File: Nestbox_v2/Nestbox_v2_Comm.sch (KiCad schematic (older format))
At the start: 3 parts

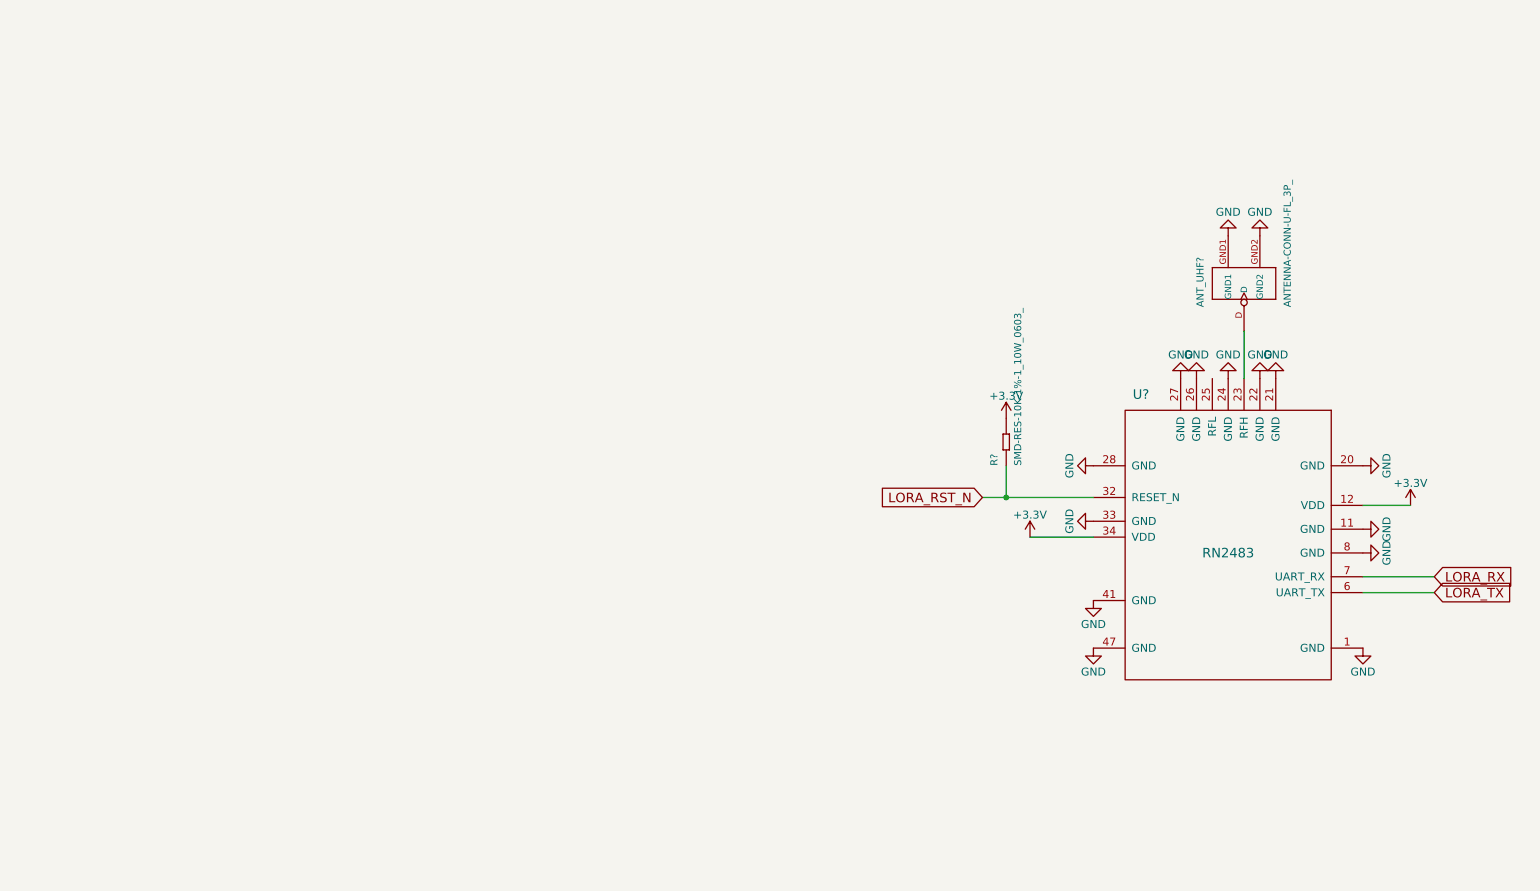
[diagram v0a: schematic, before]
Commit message: Adds XBee module to Communication schematic
The XBee module would be used for local data transfer, from a Nestbox to a
computer. This would allow data readout without the need to physically access
the box.
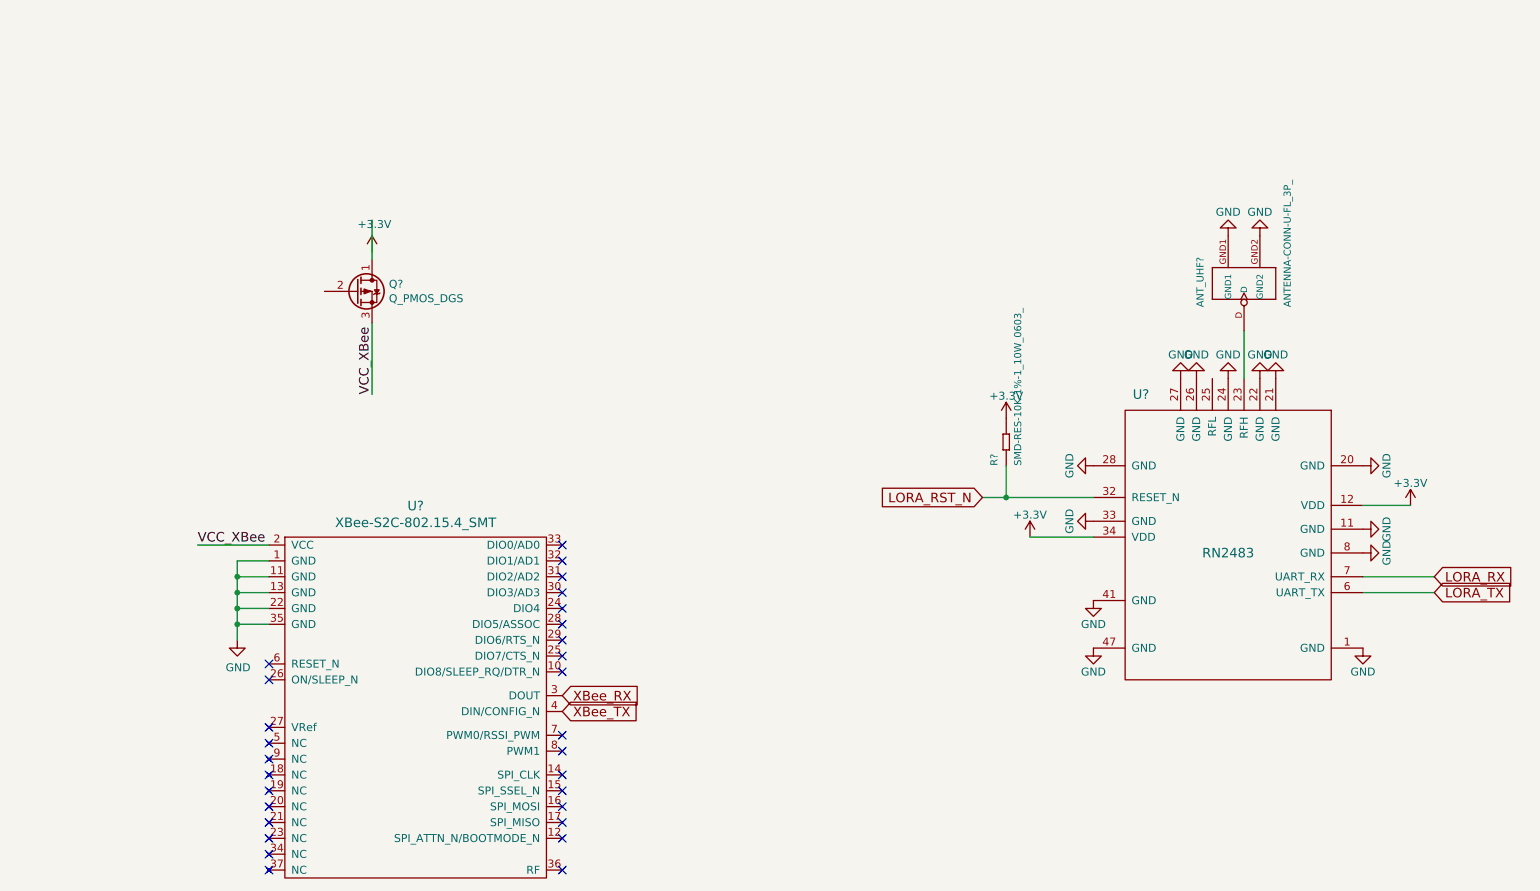
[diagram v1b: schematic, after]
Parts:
- added Q?: Q_PMOS_DGS, symbol Q_PMOS_DGS
- added U?: XBee-S2C-802.15.4_SMT, symbol XBee-S2C-802.15.4_SMT
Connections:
- net labels added: VCC_XBee, XBee_RX, XBee_TX
- wire segments 7 -> 21
- no-connect marks 0 -> 29
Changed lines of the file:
@@
 	7450 4150 7050 4150
 Wire Wire Line
-	6750 3900 7450 3900
+	6750 3900 6900 3900
+Wire Wire Line
+	6900 3900 7450 3900
 Text GLabel 6750 3900 0    60   Input ~ 0
 LORA_RST_N
@@
 	1    0    0    -1
 $EndComp
+NoConn ~ 4100 4200
+NoConn ~ 4100 4300
+NoConn ~ 4100 4400
+NoConn ~ 4100 4500
+NoConn ~ 4100 4600
+NoConn ~ 4100 4700
+NoConn ~ 4100 4800
+NoConn ~ 4100 4900
+NoConn ~ 4100 5000
+NoConn ~ 4100 5400
+NoConn ~ 4100 5500
+NoConn ~ 4100 5650
+NoConn ~ 4100 5750
+NoConn ~ 4100 5850
+NoConn ~ 4100 5950
+NoConn ~ 4100 6050
+NoConn ~ 4100 6250
+NoConn ~ 2250 5450
+NoConn ~ 2250 5550
+NoConn ~ 2250 5650
+NoConn ~ 2250 5750
+NoConn ~ 2250 5850
+NoConn ~ 2250 5950
+NoConn ~ 2250 6050
+NoConn ~ 2250 6150
+NoConn ~ 2250 6250
+NoConn ~ 2250 5350
+NoConn ~ 2250 5050
+NoConn ~ 2250 4950
+Wire Wire Line
+	2250 4300 2050 4300
+Wire Wire Line
+	2050 4300 2050 4400
+Wire Wire Line
+	2050 4400 2050 4500
+Wire Wire Line
+	2050 4500 2050 4600
+Wire Wire Line
+	2050 4600 2050 4700
+Wire Wire Line
+	2050 4700 2050 4800
+Wire Wire Line
+	2050 4400 2250 4400
+Wire Wire Line
+	2050 4500 2250 4500
+Connection ~ 2050 4400
+Wire Wire Line
+	2050 4600 2250 4600
+Connection ~ 2050 4500
+Wire Wire Line
+	2050 4700 2250 4700
+Connection ~ 2050 4600
+$Comp
+L GND #PWR?
+U 1 1 59FDFCD3
+P 2050 4800
+F 0 "#PWR?" H 2050 4550 50  0001 C CNN
+F 1 "GND" H 2055 4627 50  0000 C CNN
+F 2 "" H 2050 4800 50  0000 C CNN
+F 3 "" H 2050 4800 50  0000 C CNN
+	1    2050 4800
+	1    0    0    -1
+$EndComp
+Connection ~ 2050 4700
+Wire Wire Line
+	2250 4200 1800 4200
+Text Label 1800 4200 0    60   ~ 0
+VCC_XBee
+Text GLabel 4100 5150 2    60   Input ~ 0
+XBee_RX
+Text GLabel 4100 5250 2    60   Input ~ 0
+XBee_TX
+$Comp
+L XBee-S2C-802.15.4_SMT U?
+U 1 1 59FE0508
+P 2800 4100
+F 0 "U?" H 3175 4247 60  0000 C CNN
+F 1 "XBee-S2C-802.15.4_SMT" H 3175 4141 60  0000 C CNN
+F 2 "" H 2800 4100 60  0001 C CNN
+F 3 "" H 2800 4100 60  0001 C CNN
+	1    2800 4100
+	1    0    0    -1
+$EndComp
+$Comp
+L Q_PMOS_DGS Q?
+U 1 1 59FE0AF1
+P 2800 2600
+F 0 "Q?" H 3006 2646 50  0000 L CNN
+F 1 "Q_PMOS_DGS" H 3006 2555 50  0000 L CNN
+F 2 "" H 3000 2700 50  0000 C CNN
+F 3 "" H 2800 2600 50  0000 C CNN
+	1    2800 2600
+	1    0    0    -1
+$EndComp
+$Comp
+L +3.3V #PWR?
+U 1 1 59FE0C6C
+P 2900 2350
+F 0 "#PWR?" H 2900 2200 50  0001 C CNN
+F 1 "+3.3V" H 2915 2523 50  0000 C CNN
+F 2 "" H 2900 2350 50  0000 C CNN
+F 3 "" H 2900 2350 50  0000 C CNN
+	1    2900 2350
+	1    0    0    -1
+$EndComp
+Wire Wire Line
+	2900 2150 2900 2400
+Wire Wire Line
+	2900 2800 2900 3250
+Text Label 2900 3250 1    60   ~ 0
+VCC_XBee
 $EndSCHEMATC

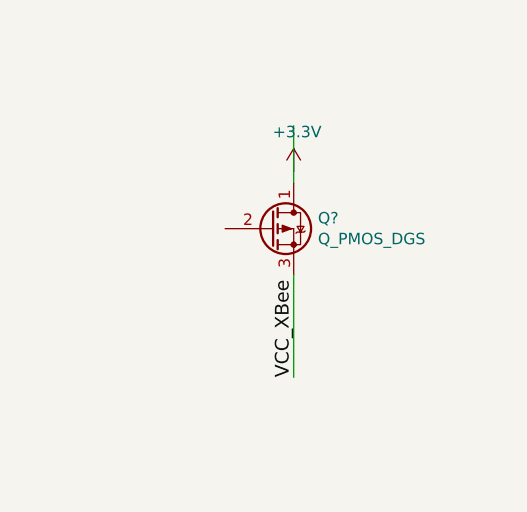
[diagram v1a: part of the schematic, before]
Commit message: Connects XBee to MSP430
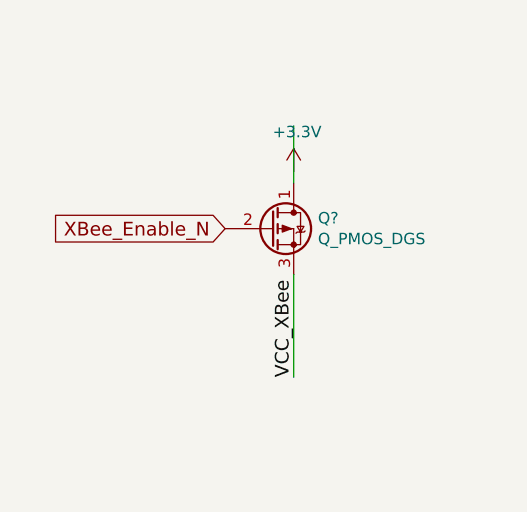
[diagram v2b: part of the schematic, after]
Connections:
- net labels added: XBee_Enable_N
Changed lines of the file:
@@
 Text Label 2900 3250 1    60   ~ 0
 VCC_XBee
+Text GLabel 2600 2600 0    60   Input ~ 0
+XBee_Enable_N
 $EndSCHEMATC

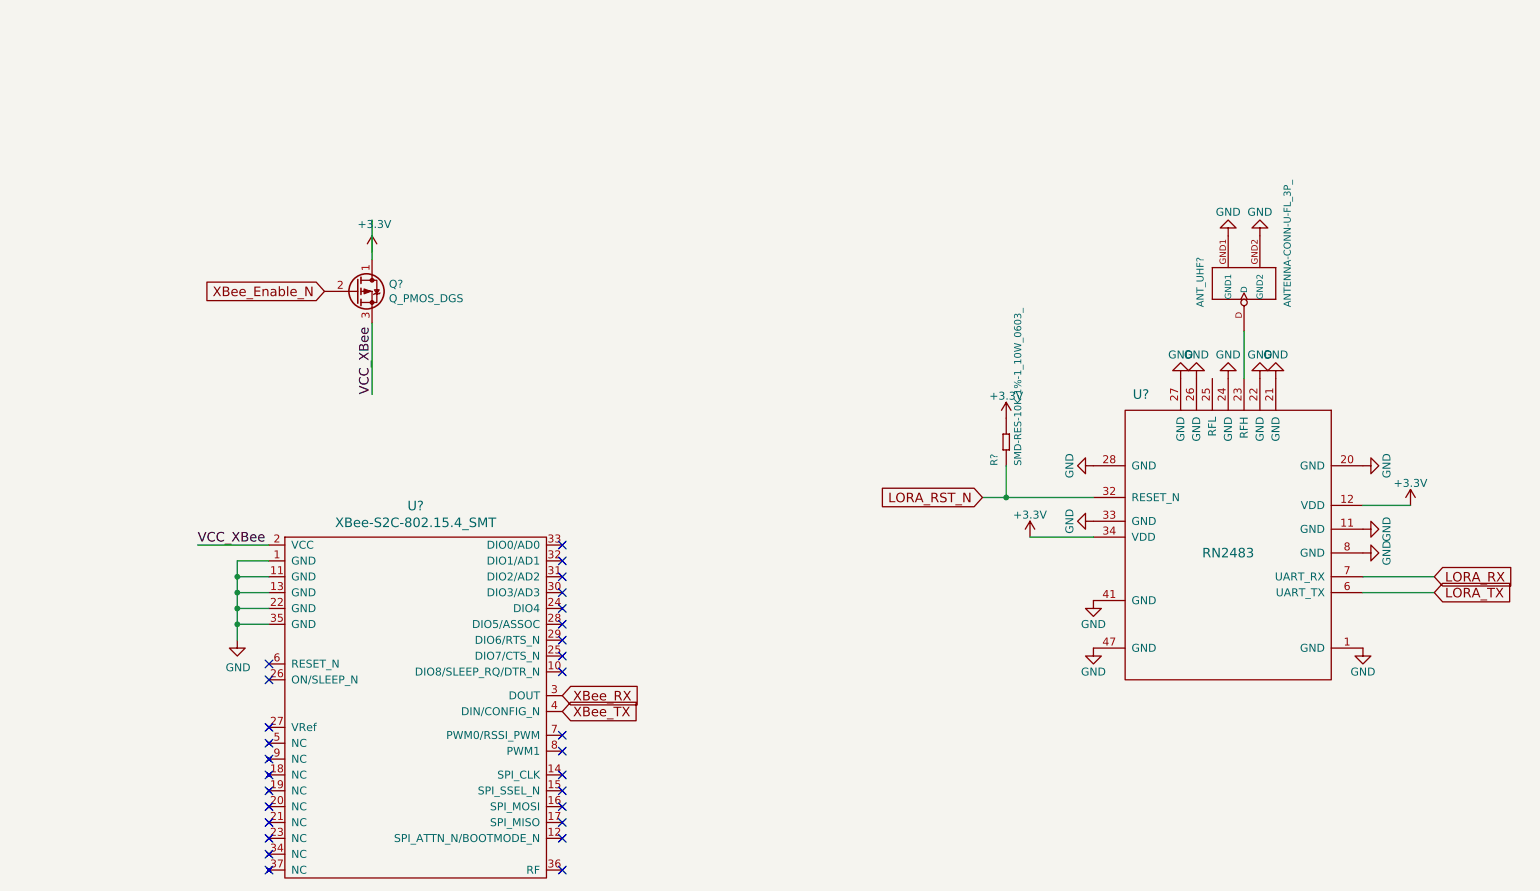
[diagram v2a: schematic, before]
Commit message: Adds ESP-12S to communication schematics
- The ESP-12S was added to the communication schematics, as an alternative to
the XBee controller.
- XBee_TX and RX signals were renamed to DATA_TX and RX
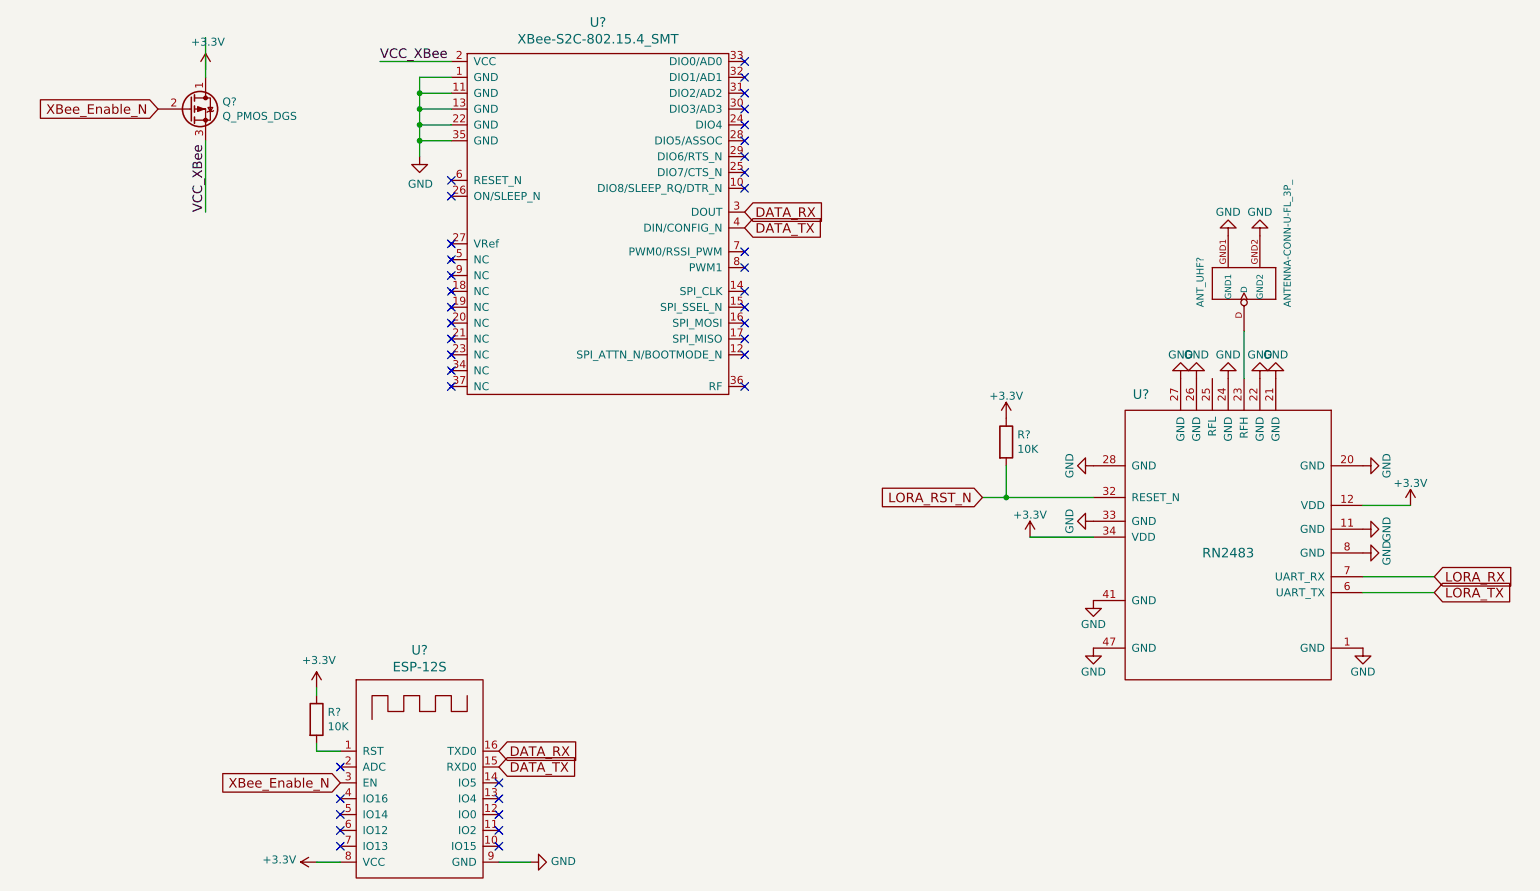
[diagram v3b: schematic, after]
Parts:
- removed R?: SMD-RES-10K-1%-1_10W_0603_, SeeedOPL-Resistor-2016:R0603, symbol SMD-RES-10K-1%-1_10W_0603_
- added R? (x2): 10K, symbol R
- added U?: ESP-12S, symbol ESP-12S
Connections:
- net labels added: DATA_RX, DATA_TX
- net labels removed: XBee_RX, XBee_TX
- no-connect marks 29 -> 39
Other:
- moved on the sheet: Q?, U?

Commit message: Renames XBee_Enable.. to more neutral Data_Enable
The XBee_Enable_N signal was renamed to Data_Enable_N as it will also be
used for the ESP8266.
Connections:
- net labels added: DATA_Enable_N
- net labels removed: XBee_Enable_N
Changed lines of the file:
@@
 VCC_XBee
 Text GLabel 1550 1450 0    60   Input ~ 0
-XBee_Enable_N
+DATA_Enable_N
 $Comp
 L R R?
@@
 $EndComp
 Text GLabel 2700 5700 0    60   Input ~ 0
-XBee_Enable_N
+DATA_Enable_N
 NoConn ~ 2700 5600
 NoConn ~ 2700 5800
